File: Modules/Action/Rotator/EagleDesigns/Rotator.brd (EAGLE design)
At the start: 100 x 80 mm, 11 parts, among them U2 ATMEGA328P_TQFP

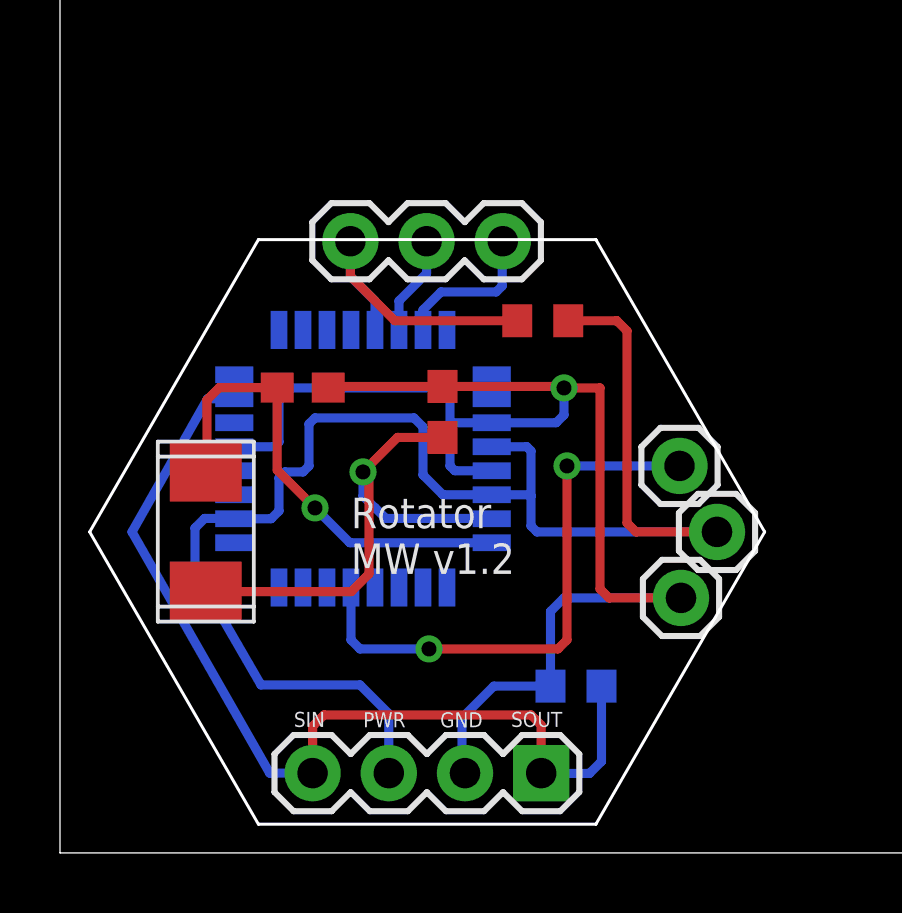
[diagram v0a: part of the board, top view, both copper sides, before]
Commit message: Rotator: removed crystal, modified to work with new bootloader #30
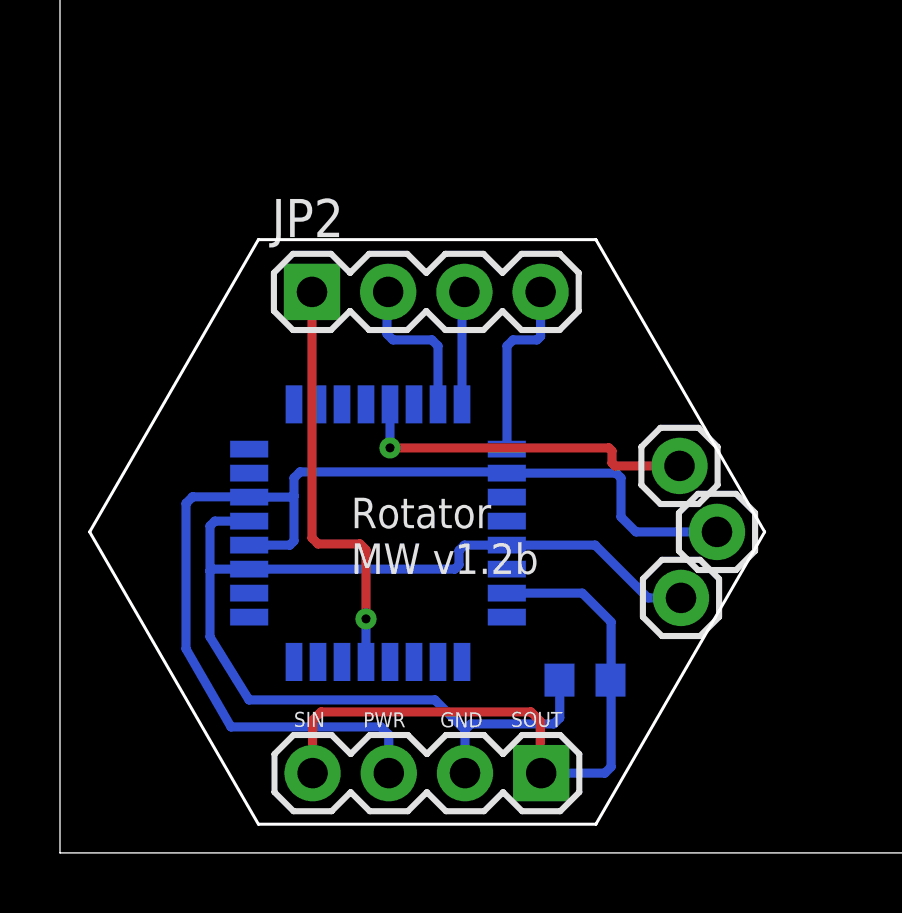
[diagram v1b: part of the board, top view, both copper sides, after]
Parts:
- removed C1, C2: 22pF, adafruit:C0603
- removed R2: 10K, resistor:R0603
- removed U$2: NX503, MakerWear:NX503
- JP2: device SparkFun-Connectors:1X03 -> SparkFun-Connectors:1X04
- moved U2 2.53 mm to (10.6, 10.7), turned to 180 degrees
- moved JP2 2.12 mm to (8.40, 18.7)
- moved R1 0.36 mm to (17.5, 5.76)
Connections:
- removed net N$1: C1.1, U$2.P$1, U2.7
- removed net N$3: C2.1, U$2.P$2, U2.8
- removed net RX: JP2.2, U2.30
- removed net TX: JP2.3, U2.31
- new net MISO: JP2.3, U2.16
- new net MOSI: JP2.2, U2.15
- new net SCK: JP2.4, U2.17
- net GND: no longer C1.2, C2.2
- net RESET: no longer R2.1
- net VCC: no longer R2.2
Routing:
- net N$1: track 17.7 -> 0.00 mm, vias 1 -> 0
- net N$3: track 15.8 -> 0.00 mm, vias 1 -> 0
- net VCC: track 50.4 -> 37.6 mm
- net GND: track 48.5 -> 38.3 mm, vias 1 -> 0
- net 1X3SIN-SOUT: track 32.4 -> 22.5 mm
- net SERVO: track 18.7 -> 11.6 mm, vias 2 -> 1
- net SCK: track 0.00 -> 6.18 mm
- net MOSI: track 0.00 -> 5.23 mm
- net TX: track 5.14 -> 0.00 mm
- net MISO: track 0.00 -> 3.78 mm
- net RX: track 3.34 -> 0.00 mm
- net RESET: track 10.6 -> 13.9 mm, vias 0 -> 1
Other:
- board text added: "Rotator MW v1.2b"
- board text removed: "Rotator MW v1.2"
